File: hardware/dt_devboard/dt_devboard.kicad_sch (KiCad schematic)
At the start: 33 parts, among them IC1 MIMXRT1015CAF4A, IC2 ESP32-C3, Y1 Crystal_GND24

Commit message: added peripheral connector sheet and doc
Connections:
- net SD_CLK: now also IC1.14 (GPIO_SD_B1_05)
- net SD_CMD: now also IC1.15 (GPIO_SD_B1_04)
- net SD_DAT2: now also IC1.17 (GPIO_SD_B1_02)
- net SD_DAT3: now also IC1.16 (GPIO_SD_B1_03)
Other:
- added sheet peripheral_conn (peripheral_conn.kicad_sch)
- note added: "Need pull-ups on SD sginals?"
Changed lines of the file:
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@@
+    (stroke (width 0) (type default) (color 0 0 0 0))
+  )
+  (wire (pts (xy 59.69 130.81) (xy 71.12 130.81))
     (stroke (width 0) (type default) (color 0 0 0 0))
   )
@@
     (stroke (width 0) (type default) (color 0 0 0 0))
   )
+  (wire (pts (xy 59.69 135.89) (xy 71.12 135.89))
+    (stroke (width 0) (type default) (color 0 0 0 0))
+  )
   (wire (pts (xy 344.17 143.51) (xy 344.17 138.43))
     (stroke (width 0) (type default) (color 0 0 0 0))
@@
     (stroke (width 0) (type default) (color 0 0 0 0))
   )
+  (wire (pts (xy 59.69 138.43) (xy 71.12 138.43))
+    (stroke (width 0) (type default) (color 0 0 0 0))
+  )
   (wire (pts (xy 306.07 138.43) (xy 306.07 140.97))
     (stroke (width 0) (type default) (color 0 0 0 0))
@@
     (stroke (width 0) (type default) (color 0 0 0 0))
   )
+  (wire (pts (xy 59.69 133.35) (xy 71.12 133.35))
+    (stroke (width 0) (type default) (color 0 0 0 0))
+  )
   (wire (pts (xy 99.06 280.67) (xy 132.08 280.67))
     (stroke (width 0) (type default) (color 0 0 0 0))
@@
   (wire (pts (xy 99.06 285.75) (xy 132.08 285.75))
     (stroke (width 0) (type default) (color 0 0 0 0))
+  )
+  (text "Need pull-ups on SD sginals?\n" (at 39.37 128.27 0)
+    (effects (font (size 1.27 1.27)) (justify left bottom))
   )
   (text "JTAG Header" (at 71.12 242.57 180)
@@
     (effects (font (size 1.27 1.27)) (justify right bottom))
   )
+  (label "SD_CLK" (at 59.69 130.81 0)
+    (effects (font (size 1.27 1.27)) (justify left bottom))
+  )
   (label "SD_DAT3" (at 179.07 274.32 0)
     (effects (font (size 1.27 1.27)) (justify left bottom))
@@
     (effects (font (size 1.27 1.27)) (justify left bottom))
   )
+  (label "SD_DAT2" (at 59.69 138.43 0)
+    (effects (font (size 1.27 1.27)) (justify left bottom))
+  )
+  (label "SD_DAT3" (at 59.69 135.89 0)
+    (effects (font (size 1.27 1.27)) (justify left bottom))
+  )
   (label "SD_CMD" (at 179.07 276.86 0)
     (effects (font (size 1.27 1.27)) (justify left bottom))
@@
   )
   (label "GPIO9" (at 341.63 215.9 90)
+    (effects (font (size 1.27 1.27)) (justify left bottom))
+  )
+  (label "SD_CMD" (at 59.69 133.35 0)
     (effects (font (size 1.27 1.27)) (justify left bottom))
   )
@@
     )
   )
+  (sheet (at 494.03 228.6) (size 29.21 49.53) (fields_autoplaced)
+    (stroke (width 0.1524) (type solid) (color 0 0 0 0))
+    (fill (color 0 0 0 0.0000))
+    (property "Sheet name" "peripheral_conn" (id 0) (at 494.03 227.8884 0)
+      (effects (font (size 1.27 1.27)) (justify left bottom))
+    )
+    (property "Sheet file" "peripheral_conn.kicad_sch" (id 1) (at 494.03 278.7146 0)
+      (effects (font (size 1.27 1.27)) (justify left top))
+    )
+  )
   (sheet (at 494.03 170.18) (size 27.94 46.99) (fields_autoplaced)
     (stroke (width 0.1524) (type solid) (color 0 0 0 0))
@@
     (path "/cfcae4a3-5d05-48fe-9a5f-9dcd4da4bd65" (page "3"))
     (path "/96116b5a-a0de-4cfe-b1e6-46c282049706" (page "4"))
+    (path "/793885b0-bfaa-4c5f-82aa-79183476bde6" (page "5"))
   )
   (symbol_instances
@@
       (reference "#PWR?") (unit 1) (value "GND") (footprint "")
     )
+    (path "/793885b0-bfaa-4c5f-82aa-79183476bde6/5c3fbc86-b745-4733-8ef5-b40aa9974c3c"
+      (reference "#PWR?") (unit 1) (value "GND") (footprint "")
+    )
+    (path "/793885b0-bfaa-4c5f-82aa-79183476bde6/607e16ab-128e-4b86-a730-5342459a2b2b"
+      (reference "#PWR?") (unit 1) (value "+3.3V") (footprint "")
+    )
+    (path "/793885b0-bfaa-4c5f-82aa-79183476bde6/b78957c1-d667-4d5c-85d2-989d524d1809"
+      (reference "#PWR?") (unit 1) (value "GND") (footprint "")
+    )
     (path "/e0e07645-12ba-4429-b7bd-9f5a31cb4b34"
       (reference "#PWR?") (unit 1) (value "+3.3V") (footprint "")
     )
+    (path "/793885b0-bfaa-4c5f-82aa-79183476bde6/ef3abe03-d68b-4855-bc8f-417487ded968"
+      (reference "#PWR?") (unit 1) (value "+3.3V") (footprint "")
+    )
     (path "/f806ebb0-0a58-44fe-90a7-d5a0f330bbfb"
       (reference "#PWR?") (unit 1) (value "GND") (footprint "")
@@
       (reference "J1") (unit 1) (value "UJ31-CH-G1-SMT-TR") (footprint "CUI_UJ31-CH-G1-SMT-TR")
     )
+    (path "/793885b0-bfaa-4c5f-82aa-79183476bde6/15613572-e2c0-4cb3-97c2-7f932dbd6ac4"
+      (reference "J?") (unit 1) (value "Conn_01x06_Female") (footprint "")
+    )
     (path "/16926dc3-0900-4302-aef5-510e031ae97e"
       (reference "J?") (unit 1) (value "Conn_ARM_JTAG_SWD_20") (footprint "")
@@
       (reference "J?") (unit 1) (value "SD_Card") (footprint "")
     )
+    (path "/793885b0-bfaa-4c5f-82aa-79183476bde6/c1cbdd6e-51f3-4b37-beed-34ae3ed00775"
+      (reference "J?") (unit 1) (value "Conn_01x06_Female") (footprint "")
+    )
     (path "/ea50380b-31ff-4c67-bd42-f26e85573f99"

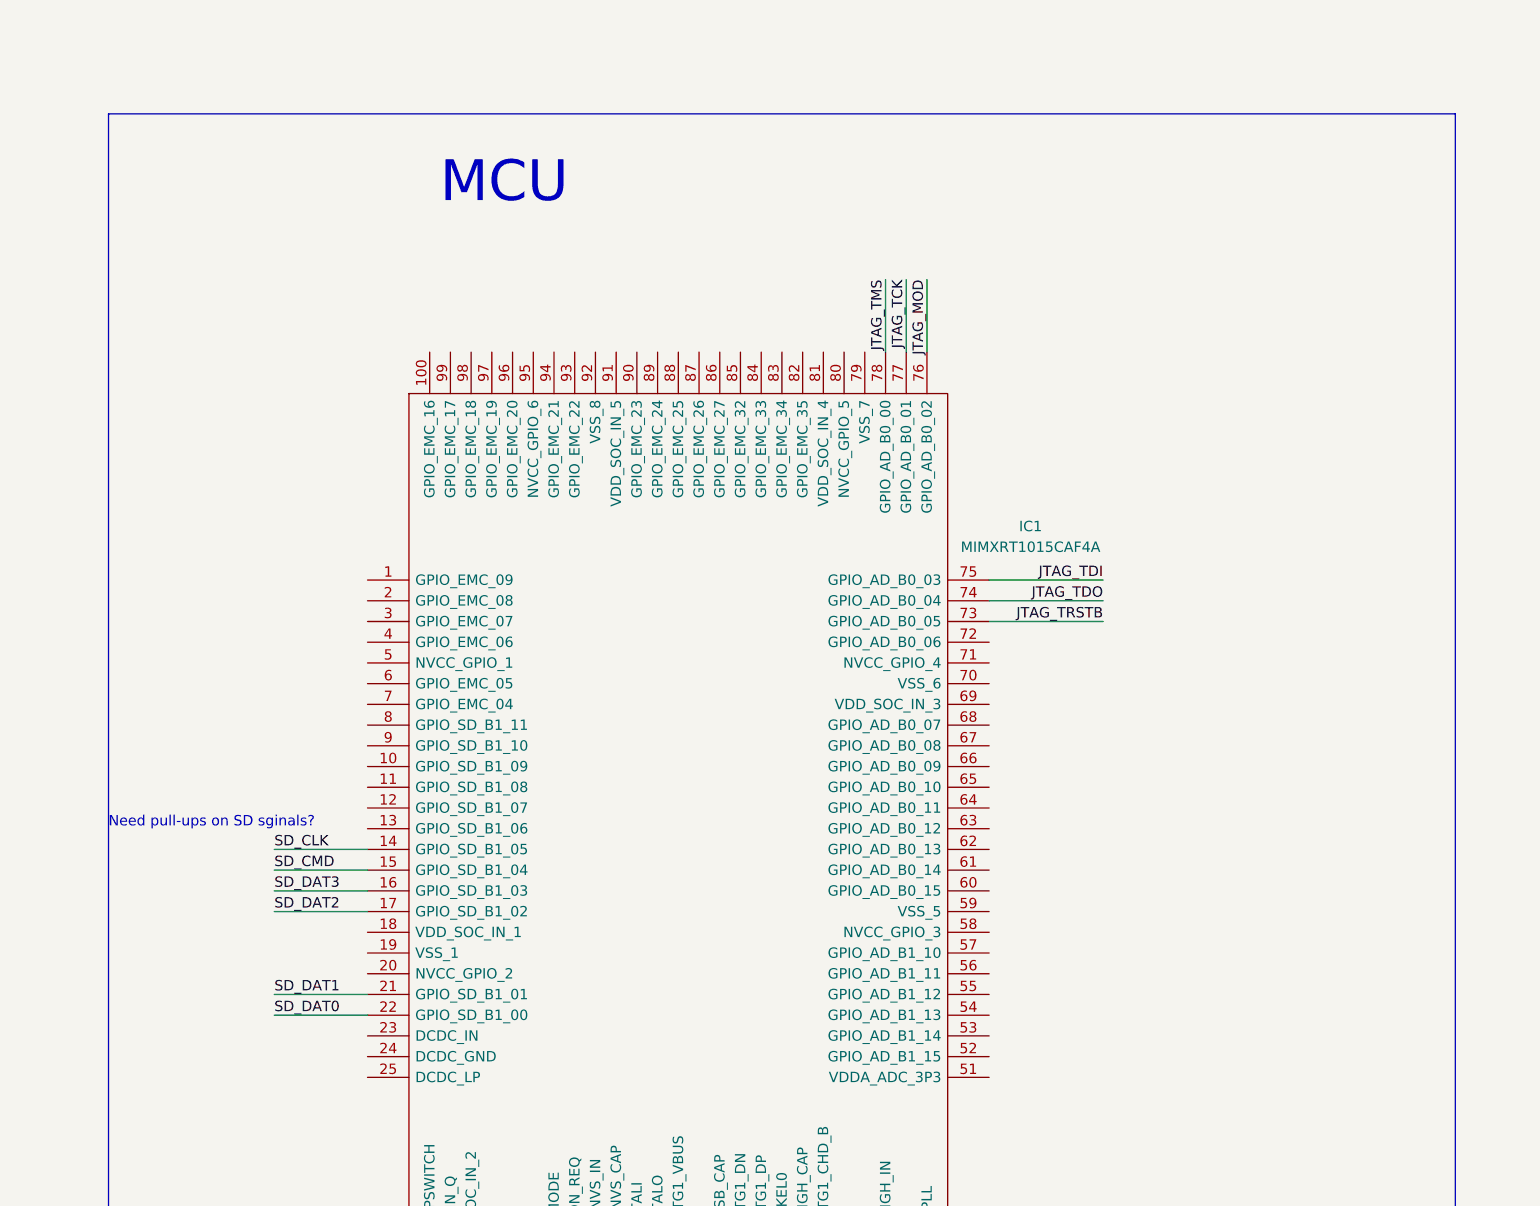
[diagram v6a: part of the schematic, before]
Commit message: added I2C, SPI and UART signals
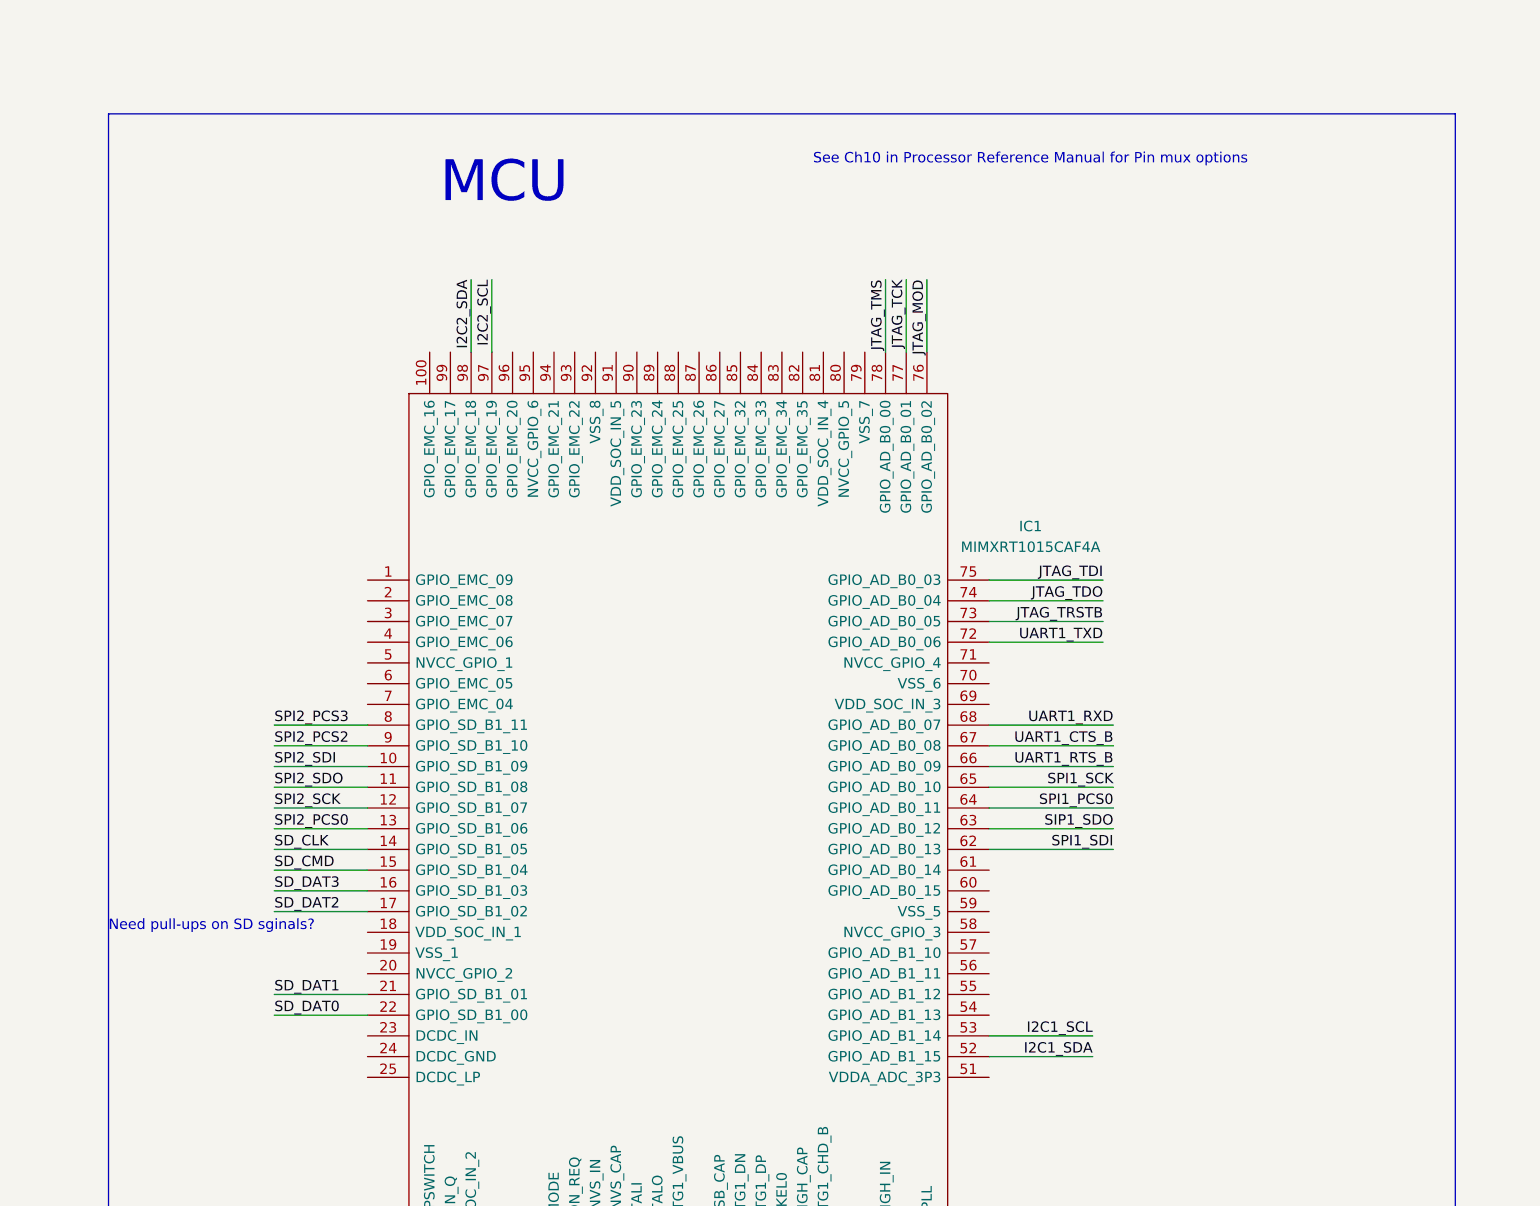
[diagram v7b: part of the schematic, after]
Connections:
- net SPI2_SDI: now reaches IC1.10 (GPIO_SD_B1_09)
- net SPI2_SDO: now reaches IC1.11 (GPIO_SD_B1_08)
- net SPI2_SCK: now reaches IC1.12 (GPIO_SD_B1_07)
- net SPI2_PCS0: now reaches IC1.13 (GPIO_SD_B1_06)
- net I2C1_SDA: now reaches IC1.52 (GPIO_AD_B1_15)
- net I2C1_SCL: now reaches IC1.53 (GPIO_AD_B1_14)
- net SPI1_SDI: now reaches IC1.62 (GPIO_AD_B0_13)
- net SIP1_SDO: now reaches IC1.63 (GPIO_AD_B0_12)
- net SPI1_PCS0: now reaches IC1.64 (GPIO_AD_B0_11)
- net SPI1_SCK: now reaches IC1.65 (GPIO_AD_B0_10)
- net UART1_RTS_B: now reaches IC1.66 (GPIO_AD_B0_09)
- net UART1_CTS_B: now reaches IC1.67 (GPIO_AD_B0_08)
- net UART1_RXD: now reaches IC1.68 (GPIO_AD_B0_07)
- net UART1_TXD: now reaches IC1.72 (GPIO_AD_B0_06)
- net SPI2_PCS3: now reaches IC1.8 (GPIO_SD_B1_11)
- net SPI2_PCS2: now reaches IC1.9 (GPIO_SD_B1_10)
- net I2C2_SCL: now reaches IC1.97 (GPIO_EMC_19)
- net I2C2_SDA: now reaches IC1.98 (GPIO_EMC_18)
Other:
- note added: "See Ch10 in Processor Reference Manual for Pin mux options"
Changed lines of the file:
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@@
+    (stroke (width 0) (type default) (color 0 0 0 0))
+  )
+  (wire (pts (xy 147.32 128.27) (xy 162.56 128.27))
     (stroke (width 0) (type default) (color 0 0 0 0))
   )
@@
     (stroke (width 0) (type default) (color 0 0 0 0))
   )
+  (wire (pts (xy 59.69 118.11) (xy 71.12 118.11))
+    (stroke (width 0) (type default) (color 0 0 0 0))
+  )
   (wire (pts (xy 400.05 179.07) (xy 400.05 182.88))
     (stroke (width 0) (type default) (color 0 0 0 0))
@@
     (stroke (width 0) (type default) (color 0 0 0 0))
   )
+  (wire (pts (xy 147.32 105.41) (xy 161.29 105.41))
+    (stroke (width 0) (type default) (color 0 0 0 0))
+  )
   (wire (pts (xy 328.93 201.93) (xy 328.93 215.9))
     (stroke (width 0) (type default) (color 0 0 0 0))
@@
     (stroke (width 0) (type default) (color 0 0 0 0))
   )
+  (wire (pts (xy 59.69 128.27) (xy 71.12 128.27))
+    (stroke (width 0) (type default) (color 0 0 0 0))
+  )
+  (wire (pts (xy 59.69 115.57) (xy 71.12 115.57))
+    (stroke (width 0) (type default) (color 0 0 0 0))
+  )
   (wire (pts (xy 119.38 186.69) (xy 119.38 191.77))
     (stroke (width 0) (type default) (color 0 0 0 0))
@@
     (stroke (width 0) (type default) (color 0 0 0 0))
   )
+  (wire (pts (xy 59.69 120.65) (xy 71.12 120.65))
+    (stroke (width 0) (type default) (color 0 0 0 0))
+  )
   (wire (pts (xy 346.71 143.51) (xy 346.71 140.97))
     (stroke (width 0) (type default) (color 0 0 0 0))
@@
     (stroke (width 0) (type default) (color 0 0 0 0))
   )
+  (wire (pts (xy 147.32 125.73) (xy 162.56 125.73))
+    (stroke (width 0) (type default) (color 0 0 0 0))
+  )
   (wire (pts (xy 290.83 127) (xy 290.83 129.54))
     (stroke (width 0) (type default) (color 0 0 0 0))
@@
     (stroke (width 0) (type default) (color 0 0 0 0))
   )
+  (wire (pts (xy 147.32 118.11) (xy 162.56 118.11))
+    (stroke (width 0) (type default) (color 0 0 0 0))
+  )
+  (wire (pts (xy 147.32 130.81) (xy 162.56 130.81))
+    (stroke (width 0) (type default) (color 0 0 0 0))
+  )
   (wire (pts (xy 81.28 307.34) (xy 105.41 307.34))
     (stroke (width 0) (type default) (color 0 0 0 0))
@@
     (stroke (width 0) (type default) (color 0 0 0 0))
   )
+  (wire (pts (xy 86.36 60.96) (xy 86.36 69.85))
+    (stroke (width 0) (type default) (color 0 0 0 0))
+  )
   (wire (pts (xy 99.06 278.13) (xy 105.41 278.13))
     (stroke (width 0) (type default) (color 0 0 0 0))
@@
     (stroke (width 0) (type default) (color 0 0 0 0))
   )
+  (wire (pts (xy 59.69 125.73) (xy 71.12 125.73))
+    (stroke (width 0) (type default) (color 0 0 0 0))
+  )
   (wire (pts (xy 168.91 248.92) (xy 175.26 248.92))
     (stroke (width 0) (type default) (color 0 0 0 0))
@@
     (stroke (width 0) (type default) (color 0 0 0 0))
   )
+  (wire (pts (xy 147.32 123.19) (xy 162.56 123.19))
+    (stroke (width 0) (type default) (color 0 0 0 0))
+  )
   (wire (pts (xy 283.21 166.37) (xy 283.21 172.72))
     (stroke (width 0) (type default) (color 0 0 0 0))
@@
     (stroke (width 0) (type default) (color 0 0 0 0))
   )
+  (wire (pts (xy 147.32 153.67) (xy 160.02 153.67))
+    (stroke (width 0) (type default) (color 0 0 0 0))
+  )
   (wire (pts (xy 200.66 287.02) (xy 193.04 287.02))
     (stroke (width 0) (type default) (color 0 0 0 0))
@@
     (stroke (width 0) (type default) (color 0 0 0 0))
   )
+  (wire (pts (xy 147.32 156.21) (xy 160.02 156.21))
+    (stroke (width 0) (type default) (color 0 0 0 0))
+  )
   (wire (pts (xy 306.07 176.53) (xy 313.69 176.53))
     (stroke (width 0) (type default) (color 0 0 0 0))
@@
     (stroke (width 0) (type default) (color 0 0 0 0))
   )
+  (wire (pts (xy 147.32 120.65) (xy 162.56 120.65))
+    (stroke (width 0) (type default) (color 0 0 0 0))
+  )
   (polyline (pts (xy 408.94 95.25) (xy 219.71 92.71))
     (stroke (width 0) (type default) (color 0 0 0 0))
@@
     (stroke (width 0) (type default) (color 0 0 0 0))
   )
+  (wire (pts (xy 83.82 60.96) (xy 83.82 69.85))
+    (stroke (width 0) (type default) (color 0 0 0 0))
+  )
   (wire (pts (xy 400.05 190.5) (xy 400.05 194.31))
     (stroke (width 0) (type default) (color 0 0 0 0))
@@
     (stroke (width 0) (type default) (color 0 0 0 0))
   )
+  (wire (pts (xy 147.32 115.57) (xy 162.56 115.57))
+    (stroke (width 0) (type default) (color 0 0 0 0))
+  )
   (polyline (pts (xy 219.71 92.71) (xy 220.98 224.79))
     (stroke (width 0) (type default) (color 0 0 0 0))
@@
     (stroke (width 0) (type default) (color 0 0 0 0))
   )
+  (wire (pts (xy 59.69 123.19) (xy 71.12 123.19))
+    (stroke (width 0) (type default) (color 0 0 0 0))
+  )
   (wire (pts (xy 99.06 285.75) (xy 132.08 285.75))
     (stroke (width 0) (type default) (color 0 0 0 0))
   )
-  (text "Need pull-ups on SD sginals?\n" (at 39.37 128.27 0)
+  (text "Need pull-ups on SD sginals?\n" (at 39.37 140.97 0)
     (effects (font (size 1.27 1.27)) (justify left bottom))
   )
@@
     (effects (font (size 5 5)) (justify left bottom))
   )
+  (text "See Ch10 in Processor Reference Manual for Pin mux options"
+    (at 125.73 46.99 0)
+    (effects (font (size 1.27 1.27)) (justify left bottom))
+  )
   (text "Add 0 ohm resistors and DNP caps at clk\n" (at 186.69 255.27 0)
     (effects (font (size 1.27 1.27)) (justify left bottom))
@@
     (effects (font (size 1.27 1.27)) (justify right bottom))
   )
+  (label "SPI2_PCS3" (at 59.69 115.57 0)
+    (effects (font (size 1.27 1.27)) (justify left bottom))
+  )
   (label "JTAG_TMS" (at 134.62 60.96 270)
     (effects (font (size 1.27 1.27)) (justify right bottom))
   )
+  (label "I2C2_SDA" (at 83.82 60.96 270)
+    (effects (font (size 1.27 1.27)) (justify right bottom))
+  )
+  (label "SPI1_SDI" (at 162.56 130.81 180)
+    (effects (font (size 1.27 1.27)) (justify right bottom))
+  )
   (label "SD_CLK" (at 59.69 130.81 0)
     (effects (font (size 1.27 1.27)) (justify left bottom))
@@
     (effects (font (size 1.27 1.27)) (justify left bottom))
   )
+  (label "SPI2_PCS0" (at 59.69 128.27 0)
+    (effects (font (size 1.27 1.27)) (justify left bottom))
+  )
+  (label "SPI2_SDO" (at 59.69 123.19 0)
+    (effects (font (size 1.27 1.27)) (justify left bottom))
+  )
+  (label "I2C1_SDA" (at 160.02 156.21 180)
+    (effects (font (size 1.27 1.27)) (justify right bottom))
+  )
+  (label "UART1_TXD" (at 161.29 105.41 180)
+    (effects (font (size 1.27 1.27)) (justify right bottom))
+  )
   (label "SPICLK" (at 373.38 166.37 180)
     (effects (font (size 1.27 1.27)) (justify right bottom))
@@
     (effects (font (size 1.27 1.27)) (justify left bottom))
   )
+  (label "SIP1_SDO" (at 162.56 128.27 180)
+    (effects (font (size 1.27 1.27)) (justify right bottom))
+  )
   (label "MTDI" (at 328.93 215.9 90)
     (effects (font (size 1.27 1.27)) (justify left bottom))
@@
     (effects (font (size 1.27 1.27)) (justify left bottom))
   )
+  (label "SPI2_SDI" (at 59.69 120.65 0)
+    (effects (font (size 1.27 1.27)) (justify left bottom))
+  )
   (label "JTAG_TCK" (at 137.16 60.96 270)
     (effects (font (size 1.27 1.27)) (justify right bottom))
@@
     (effects (font (size 1.27 1.27)) (justify right bottom))
   )
+  (label "SPI1_PCS0" (at 162.56 125.73 180)
+    (effects (font (size 1.27 1.27)) (justify right bottom))
+  )
   (label "JTAG_TRSTB" (at 132.08 270.51 180)
     (effects (font (size 1.27 1.27)) (justify right bottom))
   )
+  (label "UART1_CTS_B" (at 162.56 118.11 180)
+    (effects (font (size 1.27 1.27)) (justify right bottom))
+  )
   (label "GPIO1" (at 306.07 171.45 0)
     (effects (font (size 1.27 1.27)) (justify left bottom))
@@
     (effects (font (size 1.27 1.27)) (justify left bottom))
   )
+  (label "I2C2_SCL" (at 86.36 60.96 270)
+    (effects (font (size 1.27 1.27)) (justify right bottom))
+  )
   (label "SD_DAT3" (at 59.69 135.89 0)
     (effects (font (size 1.27 1.27)) (justify left bottom))
@@
     (effects (font (size 1.27 1.27)) (justify left bottom))
   )
+  (label "UART1_RXD" (at 162.56 115.57 180)
+    (effects (font (size 1.27 1.27)) (justify right bottom))
+  )
   (label "SD_DAT1" (at 180.34 292.1 0)
     (effects (font (size 1.27 1.27)) (justify left bottom))
@@
     (effects (font (size 1.27 1.27)) (justify left bottom))
   )
+  (label "SPI2_PCS2" (at 59.69 118.11 0)
+    (effects (font (size 1.27 1.27)) (justify left bottom))
+  )
+  (label "UART1_RTS_B" (at 162.56 120.65 180)
+    (effects (font (size 1.27 1.27)) (justify right bottom))
+  )
   (label "SD_CMD" (at 59.69 133.35 0)
     (effects (font (size 1.27 1.27)) (justify left bottom))
@@
     (effects (font (size 1.27 1.27)) (justify right bottom))
   )
+  (label "SPI2_SCK" (at 59.69 125.73 0)
+    (effects (font (size 1.27 1.27)) (justify left bottom))
+  )
   (label "JTAG_TDO" (at 161.29 100.33 180)
     (effects (font (size 1.27 1.27)) (justify right bottom))
   )
+  (label "SPI1_SCK" (at 162.56 123.19 180)
+    (effects (font (size 1.27 1.27)) (justify right bottom))
+  )
   (label "GPIO12" (at 373.38 173.99 180)
     (effects (font (size 1.27 1.27)) (justify right bottom))
@@
     (effects (font (size 1.27 1.27)) (justify right bottom))
   )
+  (label "I2C1_SCL" (at 160.02 153.67 180)
+    (effects (font (size 1.27 1.27)) (justify right bottom))
+  )
